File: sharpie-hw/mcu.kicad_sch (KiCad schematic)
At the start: 38 parts, among them J3 Conn_01x03_MountingPin, J4 Conn_01x08, SW1 SW_Push_Cross, SW2 SW_Push_Cross, SW3 SW_Push_Cross, U3 RP2350_60QFN, U4 W25Q128JVS, Y1 Crystal_GND24

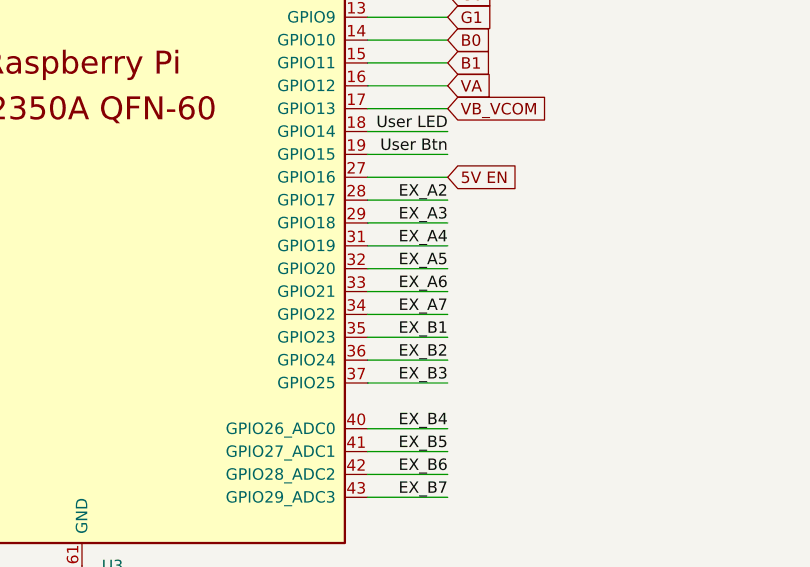
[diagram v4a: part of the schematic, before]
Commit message: Fix some BOM entries and routing choices.
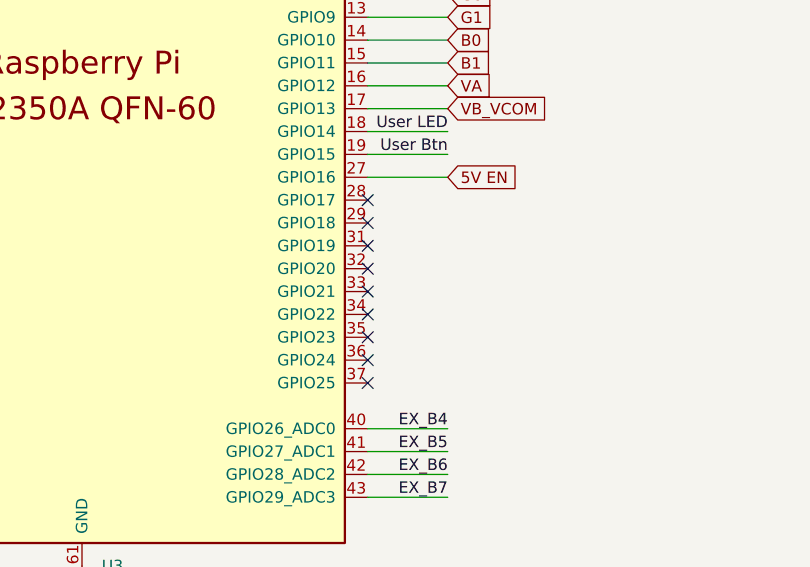
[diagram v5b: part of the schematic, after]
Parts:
- R14: JLCPCB Part # C29252 -> C25792
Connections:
- net EX_A2: no longer names the net of U3.28 (GPIO17)
- net EX_A3: no longer names the net of U3.29 (GPIO18)
- net EX_A4: no longer names the net of U3.31 (GPIO19)
- net EX_A5: no longer names the net of U3.32 (GPIO20)
- net EX_A6: no longer names the net of U3.33 (GPIO21)
- net EX_A7: no longer names the net of U3.34 (GPIO22)
- net EX_B1: no longer names the net of U3.35 (GPIO23)
- net EX_B2: no longer names the net of U3.36 (GPIO24)
- net EX_B3: no longer names the net of U3.37 (GPIO25)
- no-connect marks 0 -> 9
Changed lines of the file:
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@@
 		(color 0 0 0 0)
 	)
+	(no_connect
+		(at 180.34 123.19)
+	)
+	(no_connect
+		(at 180.34 128.27)
+	)
+	(no_connect
+		(at 180.34 130.81)
+	)
+	(no_connect
+		(at 180.34 118.11)
+	)
+	(no_connect
+		(at 180.34 115.57)
+	)
+	(no_connect
+		(at 180.34 110.49)
+	)
+	(no_connect
+		(at 180.34 113.03)
+	)
+	(no_connect
+		(at 180.34 125.73)
+	)
+	(no_connect
+		(at 180.34 120.65)
+	)
 	(wire
 		(pts
@@
 	(wire
 		(pts
-			(xy 180.34 115.57) (xy 189.23 115.57)
-		)
-		(stroke
-			(width 0)
-			(type default)
-		)
-	)
-	(wire
-		(pts
 			(xy 20.32 123.19) (xy 20.32 119.38)
 		)
@@
 	(wire
 		(pts
-			(xy 180.34 128.27) (xy 189.23 128.27)
-		)
-		(stroke
-			(width 0)
-			(type default)
-		)
-	)
-	(wire
-		(pts
 			(xy 101.6 166.37) (xy 101.6 168.91)
 		)
@@
 	(wire
 		(pts
-			(xy 180.34 120.65) (xy 189.23 120.65)
-		)
-		(stroke
-			(width 0)
-			(type default)
-		)
-	)
-	(wire
-		(pts
 			(xy 87.63 67.31) (xy 87.63 71.12)
 		)
@@
 	(wire
 		(pts
-			(xy 180.34 113.03) (xy 189.23 113.03)
-		)
-		(stroke
-			(width 0)
-			(type default)
-		)
-	)
-	(wire
-		(pts
 			(xy 139.7 179.07) (xy 139.7 186.69)
 		)
@@
 	(wire
 		(pts
-			(xy 180.34 118.11) (xy 189.23 118.11)
-		)
-		(stroke
-			(width 0)
-			(type default)
-		)
-	)
-	(wire
-		(pts
 			(xy 237.49 27.94) (xy 248.92 27.94)
 		)
@@
 	(wire
 		(pts
-			(xy 180.34 123.19) (xy 189.23 123.19)
-		)
-		(stroke
-			(width 0)
-			(type default)
-		)
-	)
-	(wire
-		(pts
 			(xy 107.95 134.62) (xy 116.84 134.62)
 		)
@@
 	(wire
 		(pts
-			(xy 180.34 125.73) (xy 189.23 125.73)
-		)
-		(stroke
-			(width 0)
-			(type default)
-		)
-	)
-	(wire
-		(pts
 			(xy 125.73 27.94) (xy 125.73 49.53)
 		)
@@
 	(wire
 		(pts
-			(xy 180.34 110.49) (xy 189.23 110.49)
-		)
-		(stroke
-			(width 0)
-			(type default)
-		)
-	)
-	(wire
-		(pts
 			(xy 186.69 35.56) (xy 198.12 35.56)
 		)
@@
 	(wire
 		(pts
-			(xy 180.34 130.81) (xy 189.23 130.81)
-		)
-		(stroke
-			(width 0)
-			(type default)
-		)
-	)
-	(wire
-		(pts
 			(xy 180.34 100.33) (xy 189.23 100.33)
 		)
@@
 		)
 	)
-	(label "EX_B1"
-		(at 189.23 125.73 180)
-		(effects
-			(font
-				(size 1.27 1.27)
-			)
-			(justify right bottom)
-		)
-	)
 	(label "EX_B5"
 		(at 189.23 138.43 180)
@@
 		)
 	)
-	(label "EX_A4"
-		(at 189.23 115.57 180)
-		(effects
-			(font
-				(size 1.27 1.27)
-			)
-			(justify right bottom)
-		)
-	)
 	(label "XOUT"
 		(at 105.41 107.95 0)
@@
 		)
 	)
-	(label "EX_A7"
-		(at 189.23 123.19 180)
-		(effects
-			(font
-				(size 1.27 1.27)
-			)
-			(justify right bottom)
-		)
-	)
 	(label "SWCLK"
 		(at 130.81 176.53 0)
@@
 		)
 	)
-	(label "EX_A5"
-		(at 189.23 118.11 180)
-		(effects
-			(font
-				(size 1.27 1.27)
-			)
-			(justify right bottom)
-		)
-	)
-	(label "EX_A2"
-		(at 189.23 110.49 180)
-		(effects
-			(font
-				(size 1.27 1.27)
-			)
-			(justify right bottom)
-		)
-	)
 	(label "User LED"
 		(at 189.23 102.87 180)
@@
 		)
 	)
-	(label "EX_B3"
-		(at 189.23 130.81 180)
-		(effects
-			(font
-				(size 1.27 1.27)
-			)
-			(justify right bottom)
-		)
-	)
 	(label "QSPI SD3"
 		(at 17.78 58.42 0)
@@
 		)
 	)
-	(label "EX_A3"
-		(at 189.23 113.03 180)
-		(effects
-			(font
-				(size 1.27 1.27)
-			)
-			(justify right bottom)
-		)
-	)
 	(label "QSPI CLK"
 		(at 17.78 48.26 0)
@@
 		)
 	)
-	(label "EX_A6"
-		(at 189.23 120.65 180)
-		(effects
-			(font
-				(size 1.27 1.27)
-			)
-			(justify right bottom)
-		)
-	)
 	(label "EX_B6"
 		(at 250.19 135.89 0)
@@
 		)
 	)
-	(label "EX_B2"
-		(at 189.23 128.27 180)
-		(effects
-			(font
-				(size 1.27 1.27)
-			)
-			(justify right bottom)
-		)
-	)
 	(global_label "BSP"
 		(shape input)
@@
 			)
 		)
-		(property "JLCPCB Part #" "C29252"
+		(property "JLCPCB Part #" "C25792"
 			(at 101.6 180.34 0)
 			(effects

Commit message: Adjust orientation of necessary parts for JLCPCB assembly.
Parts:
- L1: FT Rotation Offset (none) -> 180
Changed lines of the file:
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@@
+			)
+		)
+		(property "FT Rotation Offset" "180"
+			(at 97.79 63.5 0)
+			(effects
+				(font
+					(size 1.27 1.27)
+				)
+				(hide yes)
 			)
 		)

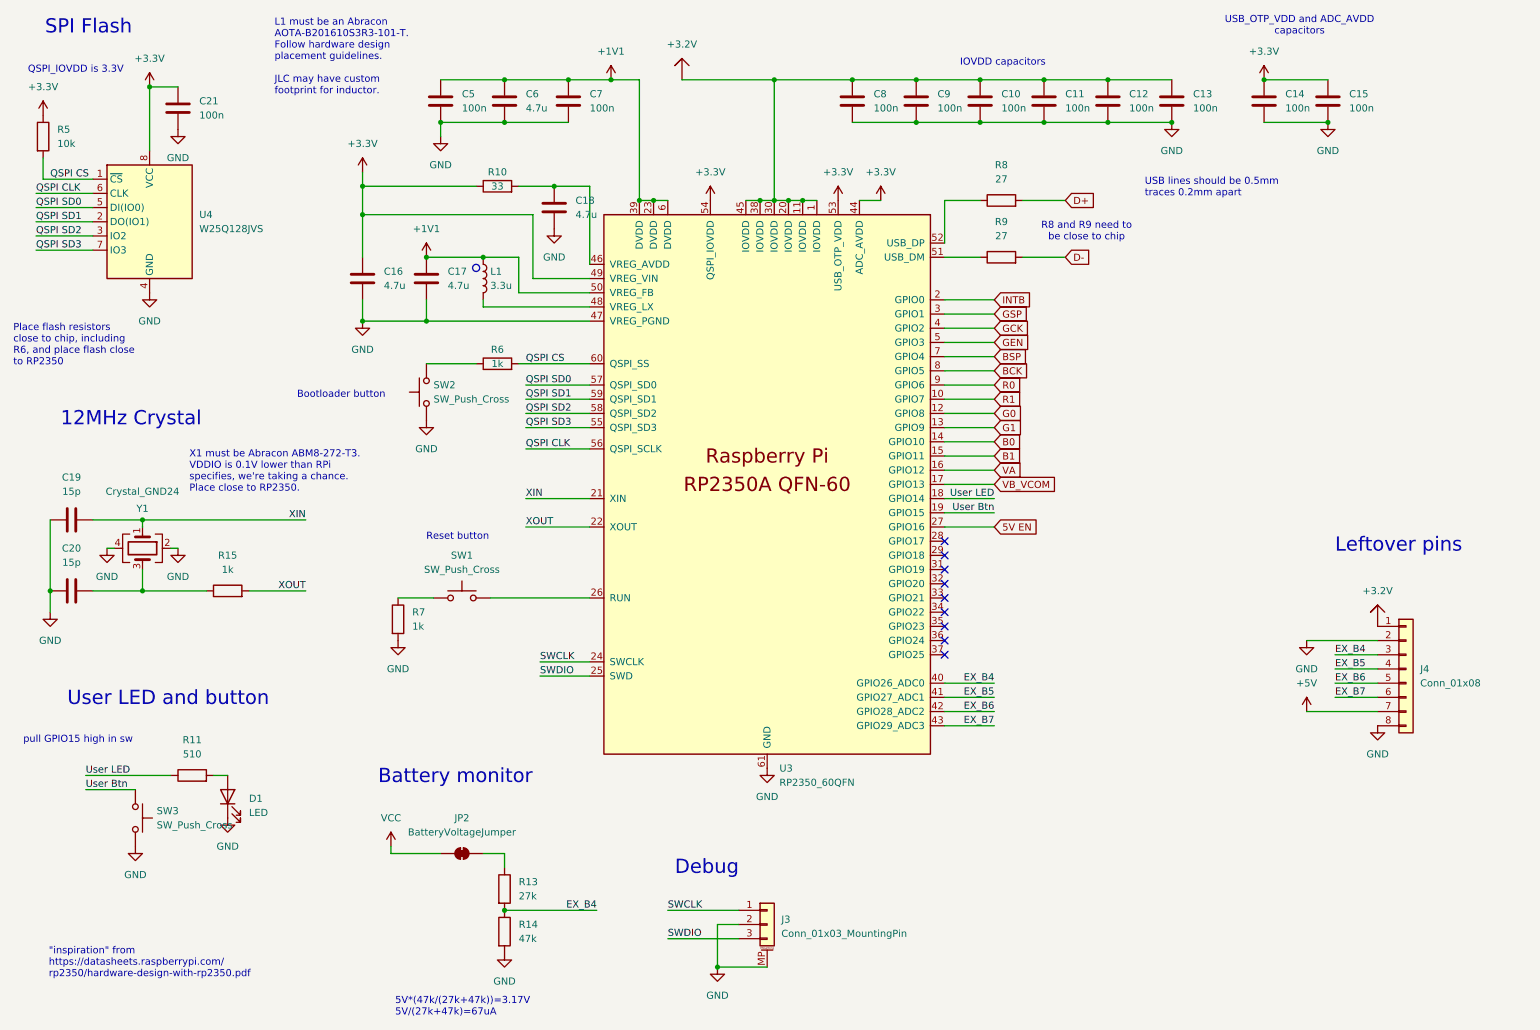
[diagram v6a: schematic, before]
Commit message: Move to as many JLCPCB basic parts as possible and remove user button.
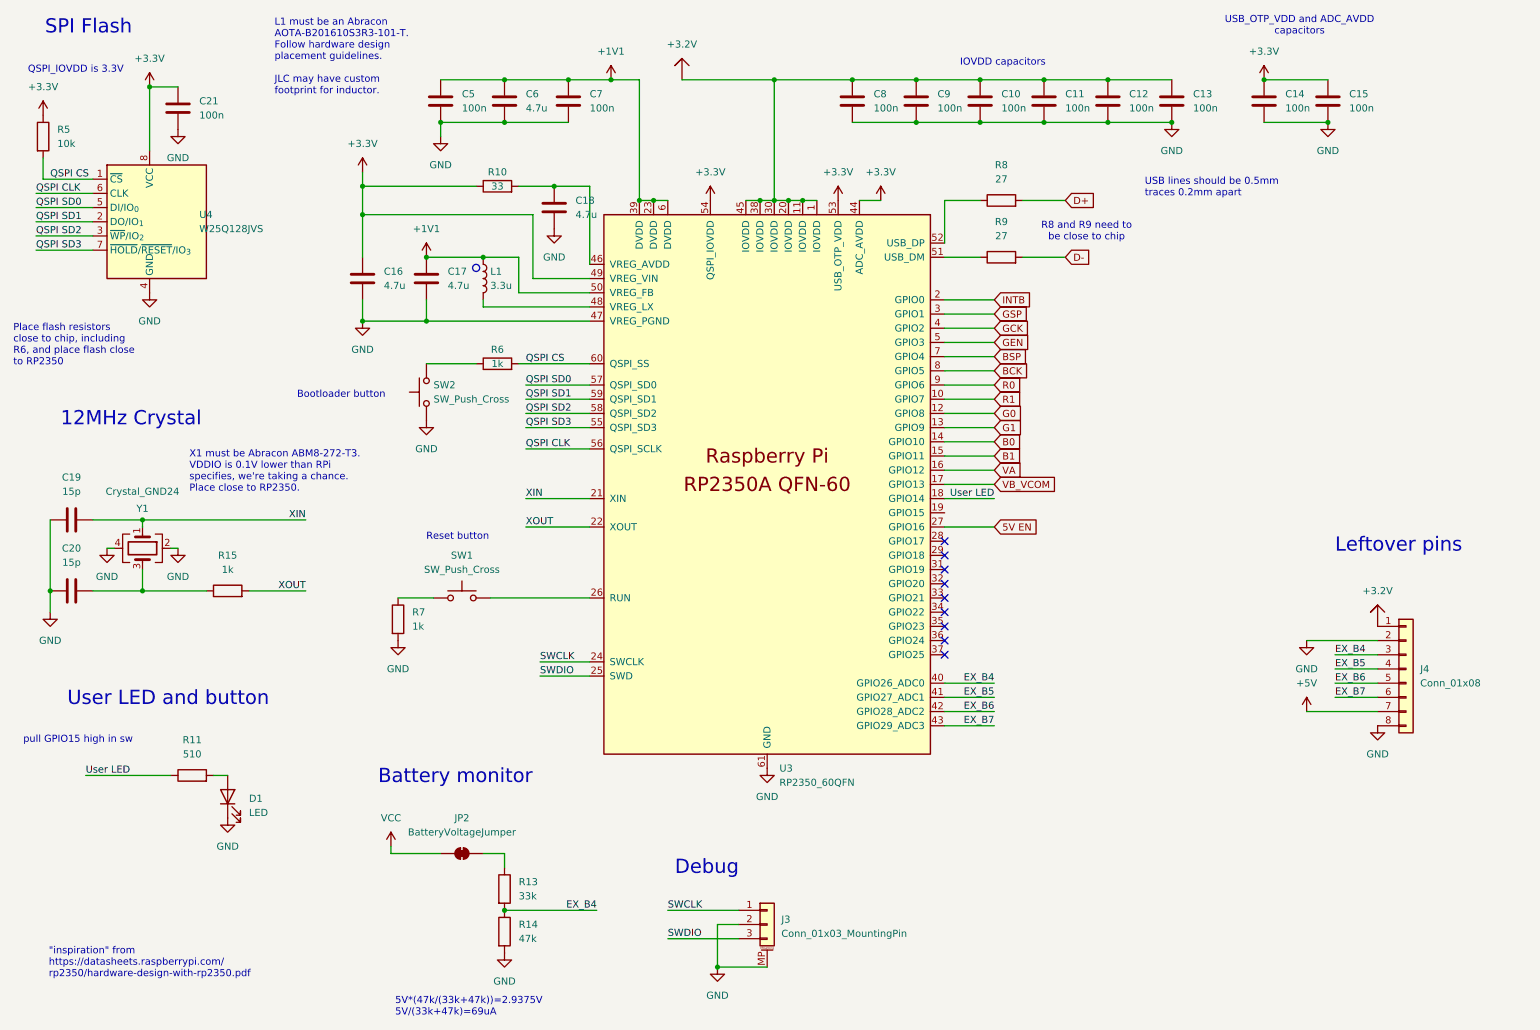
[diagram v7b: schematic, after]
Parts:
- removed SW3: SW_Push_Cross, Sharpie:KEY-SMD_4P-L4.2-W3.2-P2.20-LS4.6, symbol sharpie-hw:SW_Push_Cross
- C19, C20: JLCPCB Part # C325460 -> C1548
- D1: JLCPCB Part # C2292 -> C2297
- R13: value 27k -> 33k; JLCPCB Part # C25551 -> C25779
- R5: JLCPCB Part # C25531 -> C25744
- SW1, SW2: footprint Sharpie:KEY-SMD_4P-L4.2-W3.2-P2.20-LS4.6 -> Button_Switch_THT:SW_PUSH_6mm; JLCPCB Part # C116501 -> (none)
- U4: footprint Package_SO:SOIC-8_5.23x5.23mm_P1.27mm -> Package_SO:SOIC-8_5.3x5.3mm_P1.27mm
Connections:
- net GND: no longer SW2.2
- net at R7.1, SW1.1: no longer SW1.2
- net User Btn: no longer names the net of U3.19 (GPIO15)
- new net: R6.1, SW2.2
- new net: SW1.2, U3.26 (RUN)
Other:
- note added: "5V*(47k/(33k+47k))=2.9375V 5V/(33k+47k)=69uA"
- note removed: "5V*(47k/(27k+47k))=3.17V 5V/(27k+47k)=67uA"
- moved on the sheet: U4

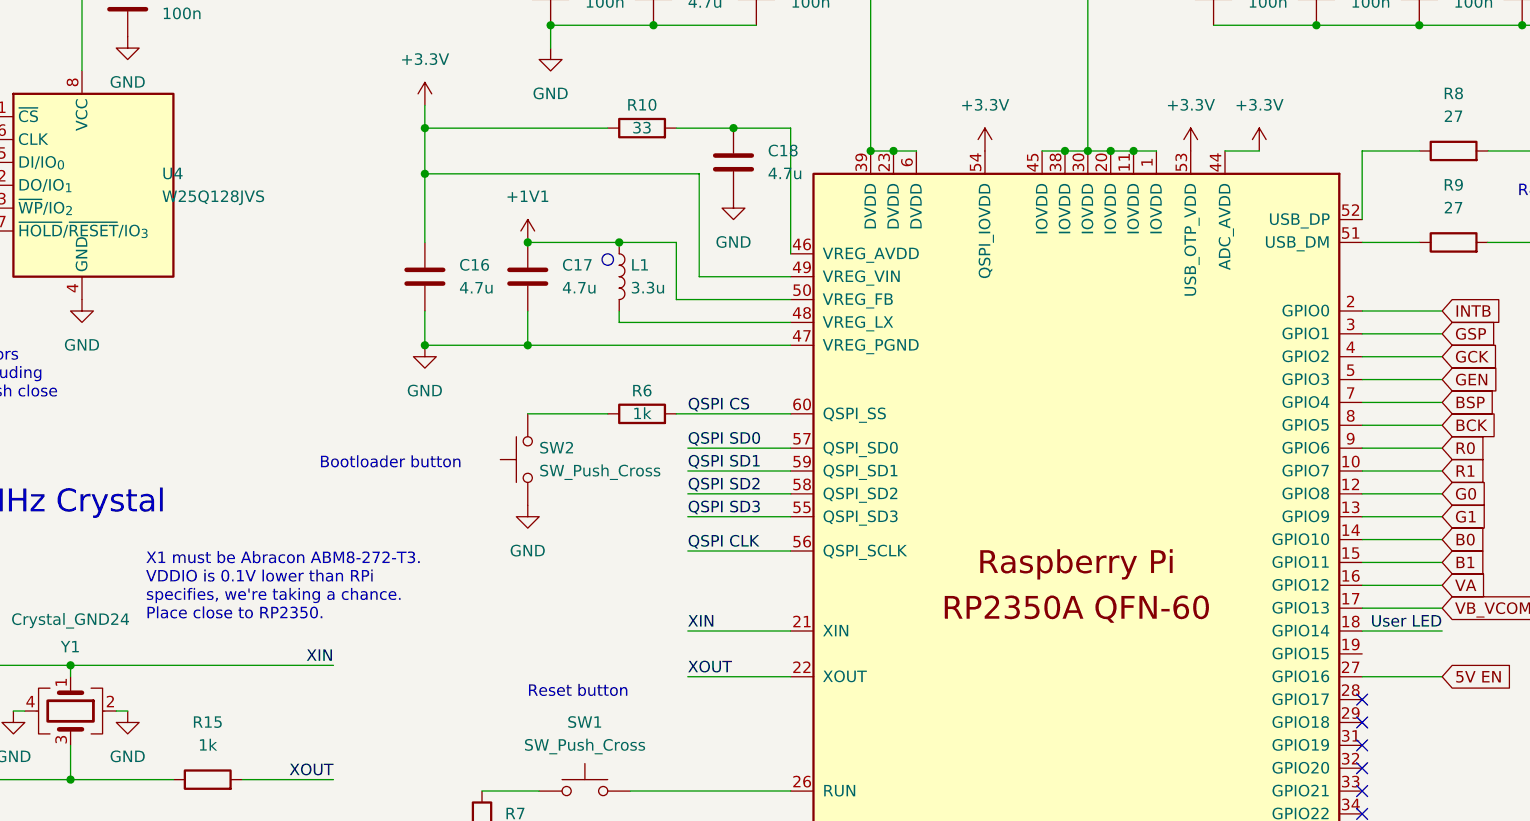
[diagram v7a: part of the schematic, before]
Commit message: Fix two items: battery connector polarity and AP3602 capacitor polarity.
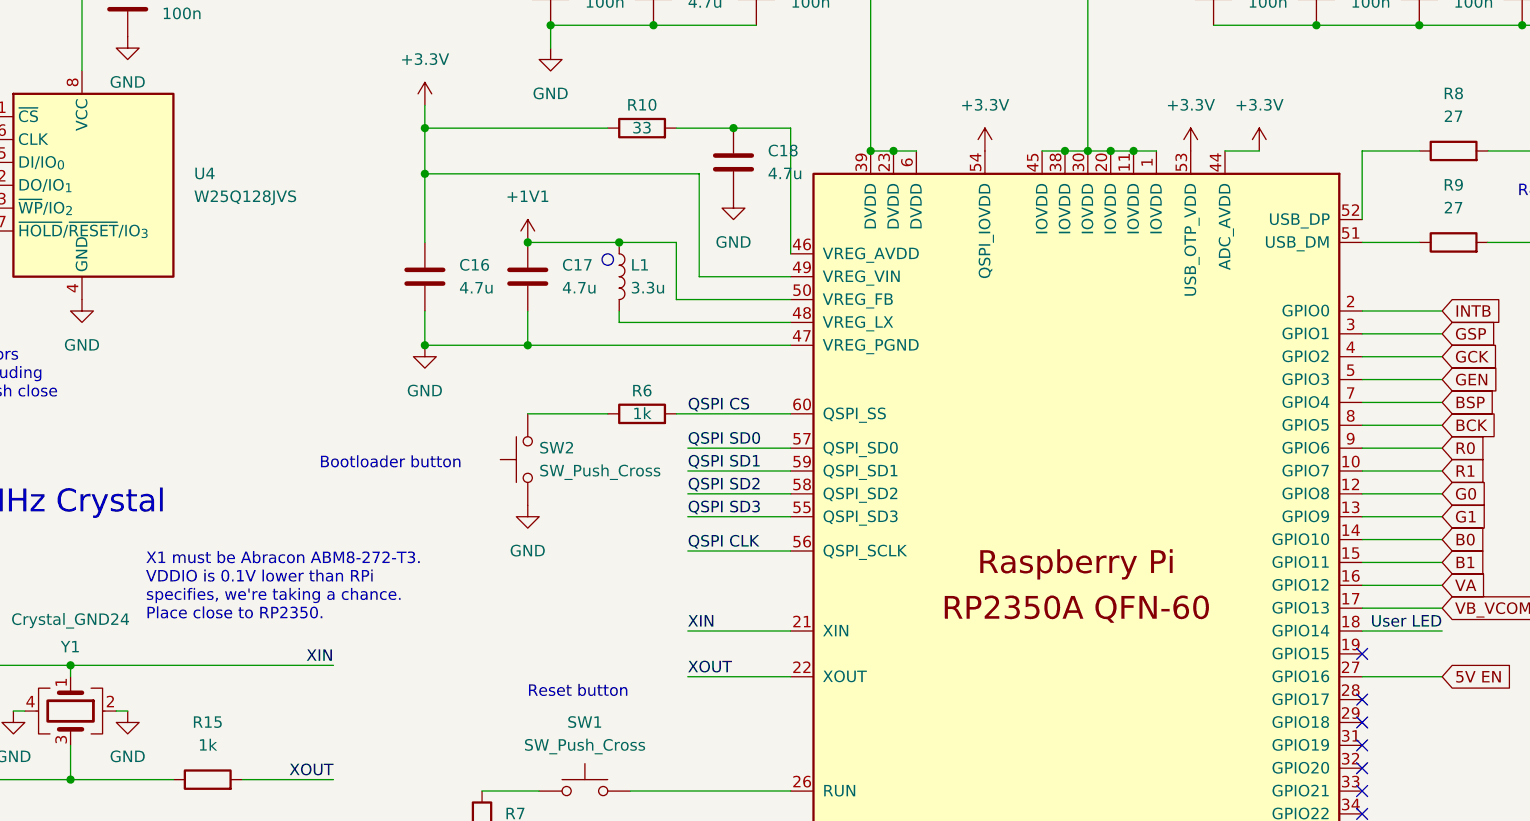
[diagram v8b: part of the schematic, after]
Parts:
- JP2: now in the parts list
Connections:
- no-connect marks 9 -> 10
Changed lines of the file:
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@@
 	)
 	(no_connect
+		(at 180.34 105.41)
+	)
+	(no_connect
 		(at 180.34 113.03)
 	)
@@
 		(unit 1)
 		(exclude_from_sim yes)
-		(in_bom no)
+		(in_bom yes)
 		(on_board yes)
 		(dnp no)
@@
 		(on_board yes)
 		(dnp no)
-		(fields_autoplaced yes)
 		(property "Reference" "U4"
-			(at 46.99 52.0699 0)
+			(at 50.546 52.07 0)
 			(effects
 				(font
@@
 		)
 		(property "Value" "W25Q128JVS"
-			(at 46.99 54.6099 0)
+			(at 50.546 54.61 0)
 			(effects
 				(font
